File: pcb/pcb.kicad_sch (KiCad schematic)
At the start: 35 parts, among them J1 Conn_01x02, J2 Conn_01x02, SW1 SW_SPDT, U1 TL072, U3 AP63205WU

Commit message: schematic v3
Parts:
- removed C11: 22u, Capacitor_SMD:C_0402_1005Metric, symbol Device:C_Small
- removed C12: 10u, Capacitor_SMD:C_0402_1005Metric, symbol Device:C_Small
- removed D1, D2: 1N4148, symbol Device:D_Small
- removed L1: 4u7, Resistor_SMD:R_0402_1005Metric, symbol Device:L_Small
- removed U3: AP63205WU, Package_TO_SOT_SMD:TSOT-23-6, symbol Regulator_Switching:AP63205WU
- added C13: 1u, Capacitor_SMD:C_0402_1005Metric, symbol Device:C_Small
- added R10: 4k7, Resistor_SMD:R_0402_1005Metric, symbol Device:R_Small
- added R11: 10k, Resistor_SMD:R_0402_1005Metric, symbol Device:R_Small
- added R9: 100k, Resistor_SMD:R_0402_1005Metric, symbol Device:R_Small
- added U3: LM7805_TO220, LM7805MP_NOPB:VREG_LM7805MP_NOPB, symbol Regulator_Linear:LM7805_TO220
- C10: value 22u -> 0.1u
- C9: value 100n -> 0.22u
- R1: value 1M -> 1k
- R3: value 10k -> 5k
- R6: value 4k7 -> 10k; footprint (none) -> Resistor_SMD:R_0402_1005Metric
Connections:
- net +5V: now also U3.3 (VO)
- net +9V: now also C9.1, U3.1 (VI)
- net GND: no longer C1.1, J2.1 (Pin_1)
- net GNDPWR: now also C9.2, R10.2, R9.2, U3.2 (GND)
- net at R6.2, U1.6 (-): now also RV2.2
- net at RV2.3, U1.7: now also C13.1; no longer RV1.3
- new net: C1.1, J2.1 (Pin_1)
- new net: C13.2, R11.1, R9.1
- new net: R10.1, R11.2, RV1.3
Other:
- moved on the sheet: C7, C8, R6, RV1, RV2, U1B, U2

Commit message: pcb v2
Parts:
- RV1: value 10k -> 100k
- RV2: footprint (none) -> Connector_PinHeader_2.54mm:PinHeader_1x03_P2.54mm_Vertical
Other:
- moved on the sheet: H1, H2, H3, H4
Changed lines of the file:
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@@
 	(wire
 		(pts
+			(xy 186.69 77.47) (xy 195.58 77.47)
+		)
+		(stroke
+			(width 0)
+			(type default)
+		)
+	)
+	(wire
+		(pts
 			(xy 186.69 88.9) (xy 193.04 88.9)
 		)
@@
 	(wire
 		(pts
-			(xy 186.69 77.47) (xy 195.58 77.47)
-		)
-		(stroke
-			(width 0)
-			(type default)
-		)
-	)
-	(wire
-		(pts
 			(xy 96.52 50.8) (xy 105.41 50.8)
 		)
@@
 	(symbol
 		(lib_id "Mechanical:MountingHole_Pad")
-		(at 194.31 35.56 0)
+		(at 180.34 22.86 0)
 		(unit 1)
 		(exclude_from_sim no)
@@
 		(fields_autoplaced yes)
 		(property "Reference" "H2"
-			(at 196.85 33.0199 0)
+			(at 182.88 20.3199 0)
 			(effects
 				(font
@@
 		)
 		(property "Value" "MountingHole_Pad"
-			(at 196.85 35.5599 0)
+			(at 182.88 22.8599 0)
 			(effects
 				(font
@@
 		)
 		(property "Footprint" "MountingHole:MountingHole_2.2mm_M2"
-			(at 194.31 35.56 0)
+			(at 180.34 22.86 0)
 			(effects
 				(font
@@
 		)
 		(property "Datasheet" "~"
-			(at 194.31 35.56 0)
+			(at 180.34 22.86 0)
 			(effects
 				(font
@@
 		)
 		(property "Description" "Mounting Hole with connection"
-			(at 194.31 35.56 0)
+			(at 180.34 22.86 0)
 			(effects
 				(font
@@
 	(symbol
 		(lib_id "Mechanical:MountingHole_Pad")
-		(at 194.31 41.91 0)
+		(at 180.34 29.21 0)
 		(unit 1)
 		(exclude_from_sim no)
@@
 		(fields_autoplaced yes)
 		(property "Reference" "H3"
-			(at 196.85 39.3699 0)
+			(at 182.88 26.6699 0)
 			(effects
 				(font
@@
 		)
 		(property "Value" "MountingHole_Pad"
-			(at 196.85 41.9099 0)
+			(at 182.88 29.2099 0)
 			(effects
 				(font
@@
 		)
 		(property "Footprint" "MountingHole:MountingHole_2.2mm_M2"
-			(at 194.31 41.91 0)
+			(at 180.34 29.21 0)
 			(effects
 				(font
@@
 		)
 		(property "Datasheet" "~"
-			(at 194.31 41.91 0)
+			(at 180.34 29.21 0)
 			(effects
 				(font
@@
 		)
 		(property "Description" "Mounting Hole with connection"
-			(at 194.31 41.91 0)
+			(at 180.34 29.21 0)
 			(effects
 				(font
@@
 	(symbol
 		(lib_id "Mechanical:MountingHole_Pad")
-		(at 194.31 29.21 0)
+		(at 180.34 16.51 0)
 		(unit 1)
 		(exclude_from_sim no)
@@
 		(fields_autoplaced yes)
 		(property "Reference" "H1"
-			(at 196.85 26.6699 0)
+			(at 182.88 13.9699 0)
 			(effects
 				(font
@@
 		)
 		(property "Value" "MountingHole_Pad"
-			(at 196.85 29.2099 0)
+			(at 182.88 16.5099 0)
 			(effects
 				(font
@@
 		)
 		(property "Footprint" "MountingHole:MountingHole_2.2mm_M2"
-			(at 194.31 29.21 0)
+			(at 180.34 16.51 0)
 			(effects
 				(font
@@
 		)
 		(property "Datasheet" "~"
-			(at 194.31 29.21 0)
+			(at 180.34 16.51 0)
 			(effects
 				(font
@@
 		)
 		(property "Description" "Mounting Hole with connection"
-			(at 194.31 29.21 0)
+			(at 180.34 16.51 0)
 			(effects
 				(font
@@
 			)
 		)
-		(property "Value" "10k"
+		(property "Value" "100k"
 			(at 175.26 64.77 90)
 			(effects
@@
 	(symbol
 		(lib_id "Mechanical:MountingHole_Pad")
-		(at 194.31 48.26 0)
+		(at 180.34 35.56 0)
 		(unit 1)
 		(exclude_from_sim no)
@@
 		(fields_autoplaced yes)
 		(property "Reference" "H4"
-			(at 196.85 45.7199 0)
+			(at 182.88 33.0199 0)
 			(effects
 				(font
@@
 		)
 		(property "Value" "MountingHole_Pad"
-			(at 196.85 48.2599 0)
+			(at 182.88 35.5599 0)
 			(effects
 				(font
@@
 		)
 		(property "Footprint" "MountingHole:MountingHole_2.2mm_M2"
-			(at 194.31 48.26 0)
+			(at 180.34 35.56 0)
 			(effects
 				(font
@@
 		)
 		(property "Datasheet" "~"
-			(at 194.31 48.26 0)
+			(at 180.34 35.56 0)
 			(effects
 				(font
@@
 		)
 		(property "Description" "Mounting Hole with connection"
-			(at 194.31 48.26 0)
+			(at 180.34 35.56 0)
 			(effects
 				(font
@@
 			)
 		)
-		(property "Footprint" ""
+		(property "Footprint" "Connector_PinHeader_2.54mm:PinHeader_1x03_P2.54mm_Vertical"
 			(at 142.24 80.01 0)
 			(effects

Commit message: change caps, do bom, reroute, readme, ship, etc
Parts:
- C1: LCSC C1525 -> C14445
- C10: value 0.1u -> 100n; LCSC (none) -> C1525
- C13: LCSC (none) -> C14445
- C2, C8: LCSC (none) -> C23733
- C3, C5: LCSC (none) -> C1525
- C4, C6: footprint Capacitor_SMD:C_0402_1005Metric -> Capacitor_SMD:C_0805_2012Metric; LCSC (none) -> C1954938
- C7: footprint Capacitor_SMD:C_0402_1005Metric -> Capacitor_SMD:C_1206_3216Metric; LCSC (none) -> C883598
- C9: LCSC (none) -> C16772
- H1, H2, H3, H4: now not fitted
- J1, J2, RV1, RV2, U1: now not fitted; now left out of the parts list
- R10: LCSC (none) -> C25900
- R11, R4, R6: LCSC (none) -> C25744
- R2, R7, R8, R9: LCSC (none) -> C25741
- R3: value 5k -> 4k7; LCSC (none) -> C25900
- R5: LCSC (none) -> C25767
- U2: value ~ -> BT; now not fitted; now left out of the parts list
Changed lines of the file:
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@@
 		(unit 1)
 		(exclude_from_sim no)
-		(in_bom yes)
+		(in_bom no)
 		(on_board yes)
-		(dnp no)
+		(dnp yes)
 		(fields_autoplaced yes)
 		(property "Reference" "J2"
@@
 		(unit 1)
 		(exclude_from_sim no)
-		(in_bom yes)
+		(in_bom no)
 		(on_board yes)
-		(dnp no)
+		(dnp yes)
 		(fields_autoplaced yes)
 		(property "Reference" "J1"
@@
 			)
 		)
+		(property "LCSC" "C25741"
+			(at 78.74 29.21 0)
+			(effects
+				(font
+					(size 1.27 1.27)
+				)
+				(hide yes)
+			)
+		)
 		(pin "1"
 		)
@@
 		(in_bom no)
 		(on_board yes)
-		(dnp no)
+		(dnp yes)
 		(fields_autoplaced yes)
 		(property "Reference" "H2"
@@
 		(unit 3)
 		(exclude_from_sim no)
-		(in_bom yes)
+		(in_bom no)
 		(on_board yes)
-		(dnp no)
+		(dnp yes)
 		(fields_autoplaced yes)
 		(property "Reference" "U1"
@@
 			)
 		)
+		(property "LCSC" "C25741"
+			(at 154.94 73.66 0)
+			(effects
+				(font
+					(size 1.27 1.27)
+				)
+				(hide yes)
+			)
+		)
 		(pin "2"
 		)
@@
 			)
 		)
-		(property "Footprint" "Capacitor_SMD:C_0402_1005Metric"
+		(property "Footprint" "Capacitor_SMD:C_1206_3216Metric"
 			(at 186.69 91.44 0)
 			(effects
@@
 			)
 		)
+		(property "LCSC" "C883598"
+			(at 186.69 91.44 0)
+			(effects
+				(font
+					(size 1.27 1.27)
+				)
+				(hide yes)
+			)
+		)
 		(pin "2"
 		)
@@
 			)
 		)
+		(property "LCSC" "C23733"
+			(at 186.69 81.28 0)
+			(effects
+				(font
+					(size 1.27 1.27)
+				)
+				(hide yes)
+			)
+		)
 		(pin "1"
 		)
@@
 		(unit 1)
 		(exclude_from_sim no)
-		(in_bom yes)
+		(in_bom no)
 		(on_board yes)
-		(dnp no)
+		(dnp yes)
 		(fields_autoplaced yes)
 		(property "Reference" "U1"
@@
 		(unit 2)
 		(exclude_from_sim no)
-		(in_bom yes)
+		(in_bom no)
 		(on_board yes)
-		(dnp no)
+		(dnp yes)
 		(property "Reference" "U1"
 			(at 134.62 58.42 0)
@@
 			)
 		)
+		(property "LCSC" "C25741"
+			(at 52.07 71.12 0)
+			(effects
+				(font
+					(size 1.27 1.27)
+				)
+				(hide yes)
+			)
+		)
 		(pin "1"
 		)
@@
 		(in_bom no)
 		(on_board yes)
-		(dnp no)
+		(dnp yes)
 		(fields_autoplaced yes)
 		(property "Reference" "H3"
@@
 			)
 		)
-		(property "Value" "5k"
+		(property "Value" "4k7"
 			(at 60.96 77.47 90)
 			(effects
@@
 			)
 		)
+		(property "LCSC" "C25900"
+			(at 60.96 80.01 90)
+			(effects
+				(font
+					(size 1.27 1.27)
+				)
+				(hide yes)
+			)
+		)
 		(pin "1"
 		)
@@
 			)
 		)
+		(property "LCSC" "C1525"
+			(at 96.52 53.34 0)
+			(effects
+				(font
+					(size 1.27 1.27)
+				)
+				(hide yes)
+			)
+		)
 		(pin "1"
 		)
@@
 			)
 		)
+		(property "LCSC" "C25767"
+			(at 105.41 72.39 0)
+			(effects
+				(font
+					(size 1.27 1.27)
+				)
+				(hide yes)
+			)
+		)
 		(pin "1"
 		)
@@
 		(in_bom no)
 		(on_board yes)
-		(dnp no)
+		(dnp yes)
 		(fields_autoplaced yes)
 		(property "Reference" "H1"
@@
 			)
 		)
+		(property "LCSC" "C23733"
+			(at 101.6 68.58 90)
+			(effects
+				(font
+					(size 1.27 1.27)
+				)
+				(hide yes)
+			)
+		)
 		(pin "1"
 		)
@@
 			)
 		)
+		(property "LCSC" "C16772"
+			(at 139.7 38.1 0)
+			(effects
+				(font
+					(size 1.27 1.27)
+				)
+				(hide yes)
+			)
+		)
 		(pin "2"
 		)
@@
 			)
 		)
-		(property "Footprint" "Capacitor_SMD:C_0402_1005Metric"
+		(property "Footprint" "Capacitor_SMD:C_0805_2012Metric"
 			(at 105.41 53.34 0)
 			(effects
@@
 			)
 		)
+		(property "LCSC" "C1954938"
+			(at 105.41 53.34 0)
+			(effects
+				(font
+					(size 1.27 1.27)
+				)
+				(hide yes)
+			)
+		)
 		(pin "2"
 		)
@@
 			)
 		)
+		(property "LCSC" "C25741"
+			(at 78.74 36.83 0)
+			(effects
+				(font
+					(size 1.27 1.27)
+				)
+				(hide yes)
+			)
+		)
 		(pin "1"
 		)
@@
 			)
 		)
-		(property "Footprint" "Capacitor_SMD:C_0402_1005Metric"
+		(property "Footprint" "Capacitor_SMD:C_0805_2012Metric"
 			(at 105.41 80.01 0)
 			(effects
@@
 			)
 		)
+		(property "LCSC" "C1954938"
+			(at 105.41 80.01 0)
+			(effects
+				(font
+					(size 1.27 1.27)
+				)
+				(hide yes)
+			)
+		)
 		(pin "2"
 		)
@@
 			)
 		)
-		(property "Value" "0.1u"
+		(property "Value" "100n"
 			(at 162.56 39.3762 0)
 			(effects
@@
 			)
 		)
+		(property "LCSC" "C1525"
+			(at 160.02 38.1 0)
+			(effects
+				(font
+					(size 1.27 1.27)
+				)
+				(hide yes)
+			)
+		)
 		(pin "2"
 		)
@@
 			)
 		)
+		(property "LCSC" "C25744"
+			(at 160.02 68.58 90)
+			(effects
+				(font
+					(size 1.27 1.27)
+				)
+				(hide yes)
+			)
+		)
 		(pin "2"
 		)
@@
 		(unit 1)
 		(exclude_from_sim no)
-		(in_bom yes)
+		(in_bom no)
 		(on_board yes)
-		(dnp no)
+		(dnp yes)
 		(fields_autoplaced yes)
 		(property "Reference" "U2"
@@
 			)
 		)
-		(property "Value" "~"
+		(property "Value" "BT"
 			(at 213.36 81.28 0)
 			(effects
@@
 			)
 		)
+		(property "LCSC" "C25900"
+			(at 165.1 73.66 0)
+			(effects
+				(font
+					(size 1.27 1.27)
+				)
+				(hide yes)
+			)
+		)
 		(pin "2"
 		)
@@
 			)
 		)
+		(property "LCSC" "C25744"
+			(at 123.19 77.47 90)
+			(effects
+				(font
+					(size 1.27 1.27)
+				)
+				(hide yes)
+			)
+		)
 		(pin "1"
 		)
@@
 			)
 		)
+		(property "LCSC" "C14445"
+			(at 151.13 68.58 90)
+			(effects
+				(font
+					(size 1.27 1.27)
+				)
+				(hide yes)
+			)
+		)
 		(pin "2"
 		)
@@
 		(unit 1)
 		(exclude_from_sim no)
-		(in_bom yes)
+		(in_bom no)
 		(on_board yes)
-		(dnp no)
+		(dnp yes)
 		(fields_autoplaced yes)
 		(property "Reference" "RV1"
@@
 			)
 		)
+		(property "LCSC" "C1525"
+			(at 96.52 80.01 0)
+			(effects
+				(font
+					(size 1.27 1.27)
+				)
+				(hide yes)
+			)
+		)
 		(pin "1"
 		)
@@
 		(in_bom no)
 		(on_board yes)
-		(dnp no)
+		(dnp yes)
 		(fields_autoplaced yes)
 		(property "Reference" "H4"
@@
 			)
 		)
+		(property "LCSC" "C25744"
+			(at 72.39 80.01 90)
+			(effects
+				(font
+					(size 1.27 1.27)
+				)
+				(hide yes)
+			)
+		)
 		(pin "1"
 		)
@@
 		(unit 1)
 		(exclude_from_sim no)
-		(in_bom yes)
+		(in_bom no)
 		(on_board yes)
-		(dnp no)
+		(dnp yes)
 		(fields_autoplaced yes)
 		(property "Reference" "RV2"
@@
 			)
 		)
-		(property "LCSC" "C1525"
+		(property "LCSC" "C14445"
 			(at 48.26 66.04 90)
 			(effects

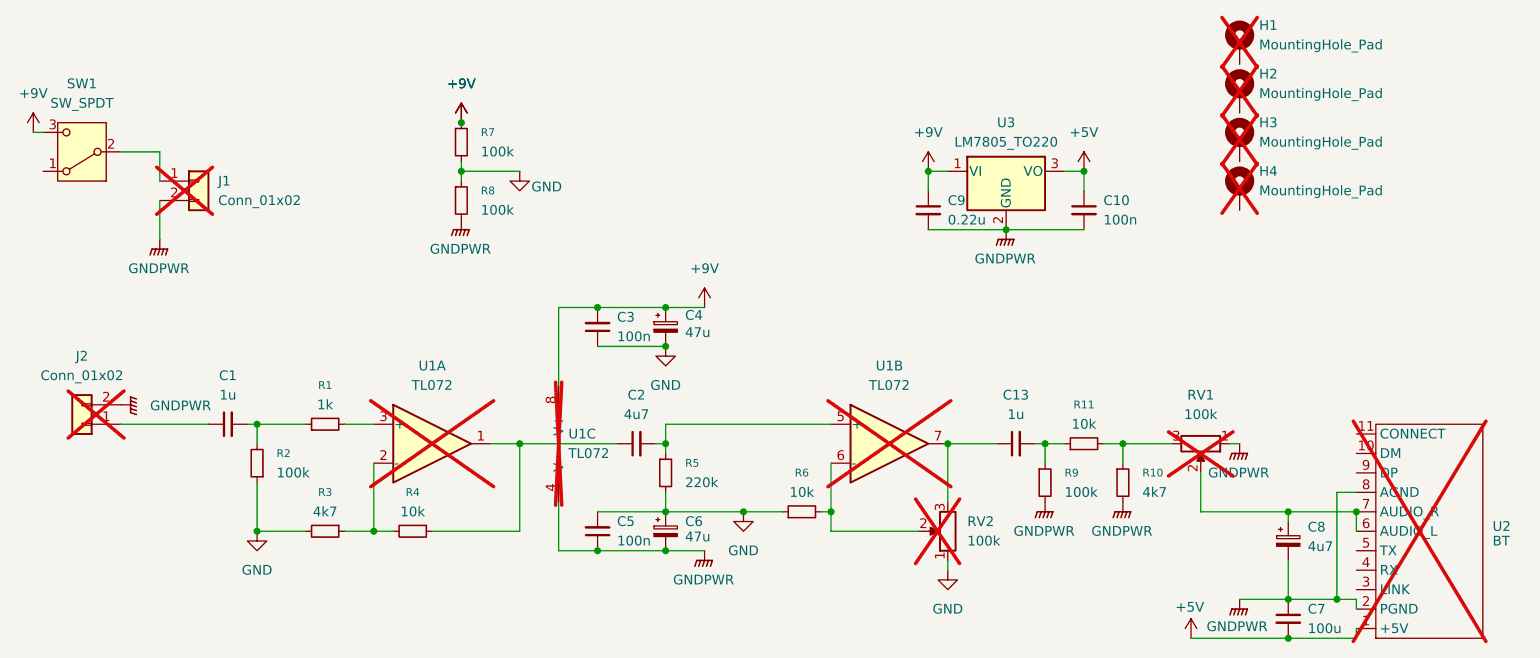
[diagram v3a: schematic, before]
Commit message: connect button footprint
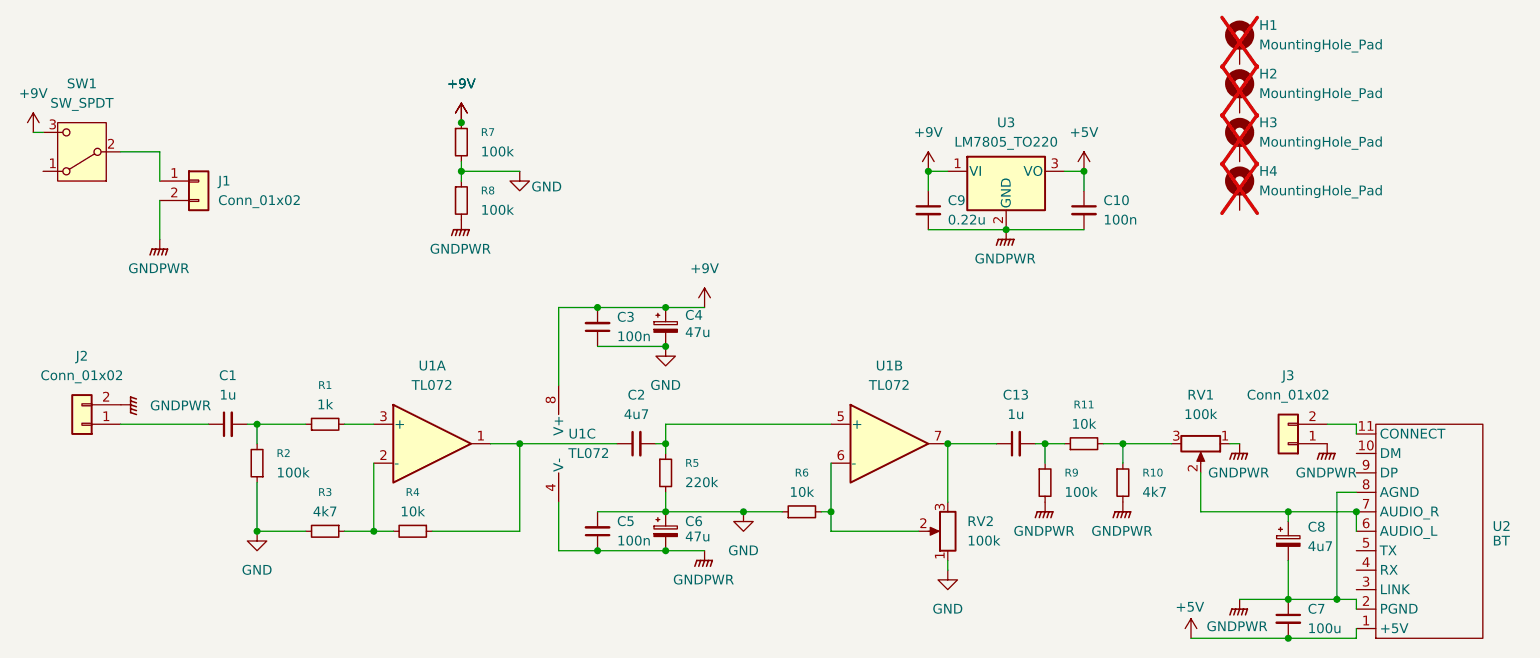
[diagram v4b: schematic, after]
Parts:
- added J3: Conn_01x02, Connector_PinHeader_2.54mm:PinHeader_1x02_P2.54mm_Vertical, symbol Connector_Generic:Conn_01x02
- J1, J2, RV1, RV2, U1, U2: now fitted
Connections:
- net GNDPWR: now also J3.1 (Pin_1)
- net at U2.11 (CONNECT): now also J3.2 (Pin_2)
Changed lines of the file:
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@@
 	(wire
 		(pts
+			(xy 195.58 66.04) (xy 195.58 67.31)
+		)
+		(stroke
+			(width 0)
+			(type default)
+		)
+	)
+	(wire
+		(pts
 			(xy 78.74 31.75) (xy 78.74 33.02)
 		)
@@
 	(wire
 		(pts
+			(xy 191.77 66.04) (xy 195.58 66.04)
+		)
+		(stroke
+			(width 0)
+			(type default)
+		)
+	)
+	(wire
+		(pts
 			(xy 149.86 40.64) (xy 160.02 40.64)
 		)
@@
 		(in_bom no)
 		(on_board yes)
-		(dnp yes)
+		(dnp no)
 		(fields_autoplaced yes)
 		(property "Reference" "J2"
@@
 		(in_bom no)
 		(on_board yes)
-		(dnp yes)
+		(dnp no)
 		(fields_autoplaced yes)
 		(property "Reference" "J1"
@@
 	(symbol
 		(lib_id "power:GNDPWR")
+		(at 191.77 68.58 0)
+		(unit 1)
+		(exclude_from_sim no)
+		(in_bom yes)
+		(on_board yes)
+		(dnp no)
+		(fields_autoplaced yes)
+		(property "Reference" "#PWR017"
+			(at 191.77 73.66 0)
+			(effects
+				(font
+					(size 1.27 1.27)
+				)
+				(hide yes)
+			)
+		)
+		(property "Value" "GNDPWR"
+			(at 191.643 72.39 0)
+			(effects
+				(font
+					(size 1.27 1.27)
+				)
+			)
+		)
+		(property "Footprint" ""
+			(at 191.77 69.85 0)
+			(effects
+				(font
+					(size 1.27 1.27)
+				)
+				(hide yes)
+			)
+		)
+		(property "Datasheet" ""
+			(at 191.77 69.85 0)
+			(effects
+				(font
+					(size 1.27 1.27)
+				)
+				(hide yes)
+			)
+		)
+		(property "Description" "Power symbol creates a global label with name \"GNDPWR\" , global ground"
+			(at 191.77 68.58 0)
+			(effects
+				(font
+					(size 1.27 1.27)
+				)
+				(hide yes)
+			)
+		)
+		(pin "1"
+		)
+		(instances
+			(project ""
+				(path "/fa437513-580b-4437-95f6-57bf94b875e3"
+					(reference "#PWR017")
+					(unit 1)
+				)
+			)
+		)
+	)
+	(symbol
+		(lib_id "power:GNDPWR")
 		(at 165.1 76.2 0)
 		(unit 1)
@@
 		(in_bom no)
 		(on_board yes)
-		(dnp yes)
+		(dnp no)
 		(fields_autoplaced yes)
 		(property "Reference" "U1"
@@
 		(in_bom no)
 		(on_board yes)
-		(dnp yes)
+		(dnp no)
 		(fields_autoplaced yes)
 		(property "Reference" "U1"
@@
 		(in_bom no)
 		(on_board yes)
-		(dnp yes)
+		(dnp no)
 		(property "Reference" "U1"
 			(at 134.62 58.42 0)
@@
 	)
 	(symbol
+		(lib_id "Connector_Generic:Conn_01x02")
+		(at 186.69 68.58 180)
+		(unit 1)
+		(exclude_from_sim no)
+		(in_bom no)
+		(on_board yes)
+		(dnp no)
+		(fields_autoplaced yes)
+		(property "Reference" "J3"
+			(at 186.69 59.69 0)
+			(effects
+				(font
+					(size 1.27 1.27)
+				)
+			)
+		)
+		(property "Value" "Conn_01x02"
+			(at 186.69 62.23 0)
+			(effects
+				(font
+					(size 1.27 1.27)
+				)
+			)
+		)
+		(property "Footprint" "Connector_PinHeader_2.54mm:PinHeader_1x02_P2.54mm_Vertical"
+			(at 186.69 68.58 0)
+			(effects
+				(font
+					(size 1.27 1.27)
+				)
+				(hide yes)
+			)
+		)
+		(property "Datasheet" "~"
+			(at 186.69 68.58 0)
+			(effects
+				(font
+					(size 1.27 1.27)
+				)
+				(hide yes)
+			)
+		)
+		(property "Description" "Generic connector, single row, 01x02, script generated (kicad-library-utils/schlib/autogen/connector/)"
+			(at 186.69 68.58 0)
+			(effects
+				(font
+					(size 1.27 1.27)
+				)
+				(hide yes)
+			)
+		)
+		(pin "1"
+		)
+		(pin "2"
+		)
+		(instances
+			(project ""
+				(path "/fa437513-580b-4437-95f6-57bf94b875e3"
+					(reference "J3")
+					(unit 1)
+				)
+			)
+		)
+	)
+	(symbol
 		(lib_id "VoltLibrary:BluetoothTransmitter")
 		(at 212.09 66.04 180)
@@
 		(in_bom no)
 		(on_board yes)
-		(dnp yes)
+		(dnp no)
 		(fields_autoplaced yes)
 		(property "Reference" "U2"
@@
 		(in_bom no)
 		(on_board yes)
-		(dnp yes)
+		(dnp no)
 		(fields_autoplaced yes)
 		(property "Reference" "RV1"
@@
 		(in_bom no)
 		(on_board yes)
-		(dnp yes)
+		(dnp no)
 		(fields_autoplaced yes)
 		(property "Reference" "RV2"
